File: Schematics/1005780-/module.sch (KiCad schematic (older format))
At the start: 0 parts

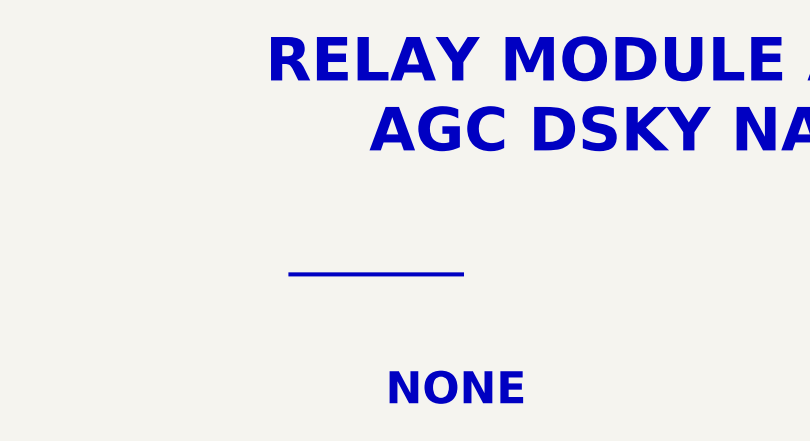
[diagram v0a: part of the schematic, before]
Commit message: Finished/proofed CAD transcription of drawing 1005780-.  Fixed a couple of related textual errors I found in drawing 1006161C as a part of that process.
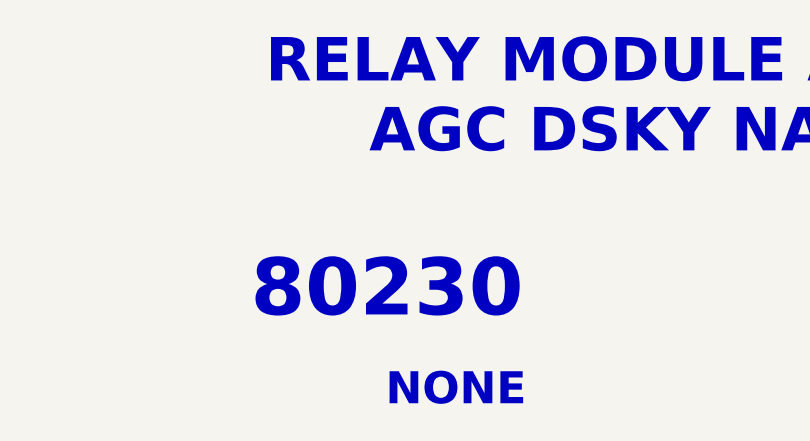
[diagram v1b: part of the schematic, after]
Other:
- note added: "80230"
- note removed: "________"
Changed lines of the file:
@@
 Text Notes 44875 33500 0    140  ~ 28
 NONE
-Text Notes 44450 32900 0    140  ~ 28
-________
+Text Notes 44285 33125 0    250  ~ 50
+80230
 $EndSCHEMATC
